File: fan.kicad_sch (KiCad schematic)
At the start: 9 parts, among them J4 Conn_01x04, U7 EMC2101

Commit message: moved all custom symbols and footprints to the bitaxe library
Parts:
- U7: symbol dayminer:EMC2101 -> bitaxe:EMC2101
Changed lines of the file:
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@@
     )
   )
-  (symbol (lib_id "dayminer:EMC2101") (at 144.78 78.105 0) (unit 1)
+  (symbol (lib_id "bitaxe:EMC2101") (at 144.78 78.105 0) (unit 1)
     (in_bom yes) (on_board yes) (dnp no)
     (property "Reference" "U7" (at 153.67 69.215 0)

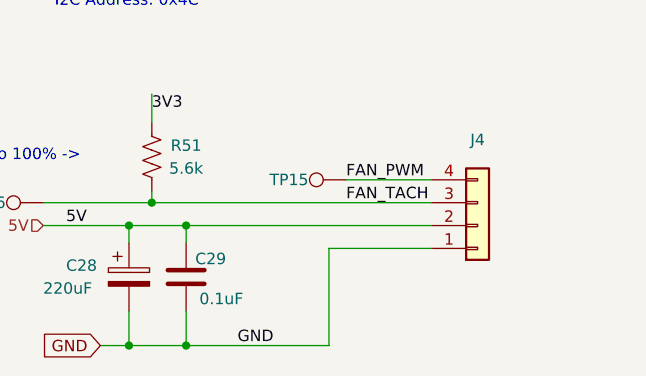
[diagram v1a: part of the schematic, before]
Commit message: Changed barrel plug to 2 pin, added JST-XH connector
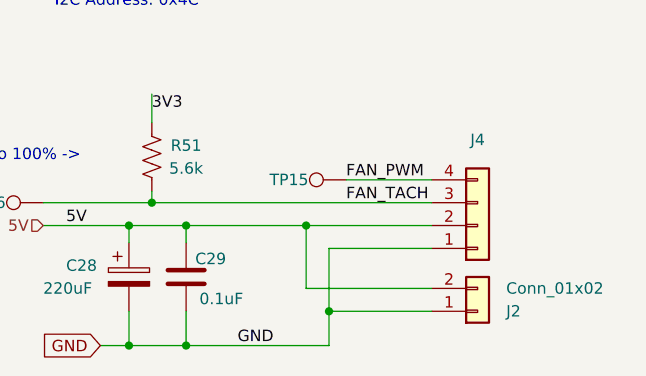
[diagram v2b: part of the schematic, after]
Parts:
- added J2: Conn_01x02, Connector_JST:JST_XH_B2B-XH-A_1x02_P2.50mm_Vertical, symbol Connector_Generic:Conn_01x02
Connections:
- net 5V: now also J2.2 (Pin_2)
- net GND: now also J2.1 (Pin_1)
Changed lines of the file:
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@@
   (junction (at 191.77 66.04) (diameter 0) (color 0 0 0 0)
   )
+  (junction (at 164.465 113.665) (diameter 0) (color 0 0 0 0)
+  )
   (junction (at 151.13 113.665) (diameter 0) (color 0 0 0 0)
+  )
+  (junction (at 167.005 123.19) (diameter 0) (color 0 0 0 0)
   )
   (junction (at 147.32 111.125) (diameter 0) (color 0 0 0 0)
@@
     (stroke (width 0) (type default))
   )
+  (wire (pts (xy 178.435 120.65) (xy 164.465 120.65))
+    (stroke (width 0) (type default))
+  )
   (wire (pts (xy 179.07 66.04) (xy 191.77 66.04))
     (stroke (width 0) (type default))
@@
     (stroke (width 0) (type default))
   )
-  (wire (pts (xy 167.005 116.205) (xy 167.005 127))
+  (wire (pts (xy 167.005 116.205) (xy 167.005 123.19))
     (stroke (width 0) (type default))
   )
@@
     (stroke (width 0) (type default))
   )
+  (wire (pts (xy 167.005 123.19) (xy 167.005 127))
+    (stroke (width 0) (type default))
+  )
+  (wire (pts (xy 167.005 123.19) (xy 178.435 123.19))
+    (stroke (width 0) (type default))
+  )
   (wire (pts (xy 191.77 81.28) (xy 191.77 83.185))
     (stroke (width 0) (type default))
@@
     (stroke (width 0) (type default))
   )
+  (wire (pts (xy 164.465 113.665) (xy 178.435 113.665))
+    (stroke (width 0) (type default))
+  )
   (wire (pts (xy 151.13 113.665) (xy 151.13 115.57))
     (stroke (width 0) (type default))
@@
     (stroke (width 0) (type default))
   )
-  (wire (pts (xy 151.13 113.665) (xy 178.435 113.665))
+  (wire (pts (xy 151.13 113.665) (xy 164.465 113.665))
     (stroke (width 0) (type default))
   )
@@
   )
   (wire (pts (xy 141.605 127) (xy 144.78 127))
+    (stroke (width 0) (type default))
+  )
+  (wire (pts (xy 164.465 120.65) (xy 164.465 113.665))
     (stroke (width 0) (type default))
   )
@@
         )
       )
+    )
+  )
+  (symbol (lib_id "Connector_Generic:Conn_01x02") (at 183.515 123.19 0) (mirror x) (unit 1)
+    (in_bom yes) (on_board yes) (dnp no)
+    (property "Reference" "J2" (at 186.69 123.19 0)
+      (effects (font (size 1.27 1.27)) (justify left))
+    )
+    (property "Value" "Conn_01x02" (at 186.69 120.65 0)
+      (effects (font (size 1.27 1.27)) (justify left))
+    )
+    (property "Footprint" "Connector_JST:JST_XH_B2B-XH-A_1x02_P2.50mm_Vertical" (at 183.515 123.19 0)
+      (effects (font (size 1.27 1.27)) hide)
+    )
+    (property "Datasheet" "https://www.jst-mfg.com/product/pdf/eng/eXH.pdf" (at 183.515 123.19 0)
+      (effects (font (size 1.27 1.27)) hide)
+    )
+    (property "DK" "https://www.digikey.com/en/products/detail/jst-sales-america-inc/B2B-XH-A/1651045" (at 183.515 123.19 0)
+      (effects (font (size 1.27 1.27)) hide)
+    )
+    (pin "1")
+    (pin "2")
+    (instances
+      (project "bitaxeUltra"
+        (path "/e63e39d7-6ac0-4ffd-8aa3-1841a4541b55/8e8832ea-6bf1-49d2-b3a5-32a207f555d2"
+          (reference "J2") (unit 1)
+        )
+      )

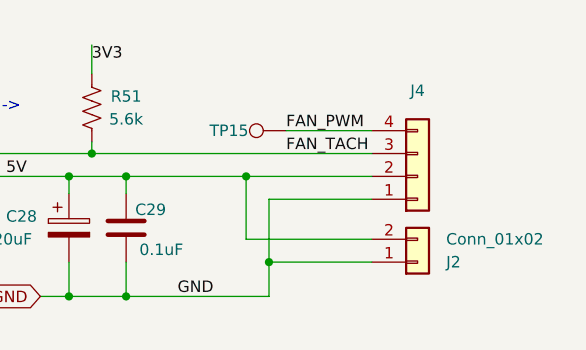
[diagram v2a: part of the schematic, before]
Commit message: fix JSX, updated boms
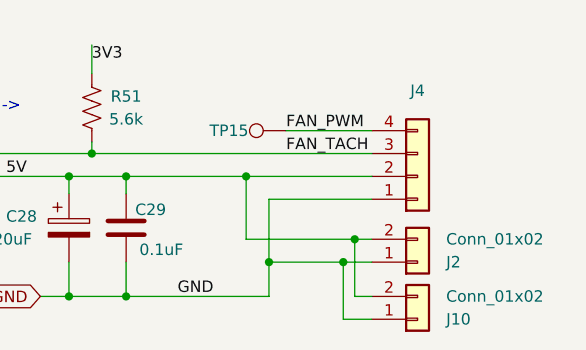
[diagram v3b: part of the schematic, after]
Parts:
- added J10: Conn_01x02, Connector_JST:JST_XH_B2B-XH-A_1x02_P2.50mm_Vertical, symbol Connector_Generic:Conn_01x02
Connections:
- net 5V: now also J10.2 (Pin_2)
- net GND: now also J10.1 (Pin_1)
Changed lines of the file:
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@@
     (rev "0")
   )
+  (junction (at 175.26 123.19) (diameter 0) (color 0 0 0 0)
+  )
   (junction (at 191.77 66.04) (diameter 0) (color 0 0 0 0)
   )
   (junction (at 164.465 113.665) (diameter 0) (color 0 0 0 0)
+  )
+  (junction (at 176.53 120.65) (diameter 0) (color 0 0 0 0)
   )
   (junction (at 151.13 113.665) (diameter 0) (color 0 0 0 0)
@@
     (stroke (width 0) (type default))
   )
-  (wire (pts (xy 178.435 120.65) (xy 164.465 120.65))
+  (wire (pts (xy 178.435 120.65) (xy 176.53 120.65))
     (stroke (width 0) (type default))
   )
@@
     (stroke (width 0) (type default))
   )
+  (wire (pts (xy 164.465 120.65) (xy 176.53 120.65))
+    (stroke (width 0) (type default))
+  )
   (wire (pts (xy 167.005 116.205) (xy 167.005 123.19))
     (stroke (width 0) (type default))
@@
     (stroke (width 0) (type default))
   )
-  (wire (pts (xy 167.005 123.19) (xy 178.435 123.19))
+  (wire (pts (xy 167.005 123.19) (xy 175.26 123.19))
     (stroke (width 0) (type default))
   )
@@
     (stroke (width 0) (type default))
   )
+  (wire (pts (xy 178.435 129.54) (xy 175.26 129.54))
+    (stroke (width 0) (type default))
+  )
   (wire (pts (xy 191.77 66.04) (xy 191.77 73.66))
     (stroke (width 0) (type default))
@@
     (stroke (width 0) (type default))
   )
+  (wire (pts (xy 175.26 123.19) (xy 178.435 123.19))
+    (stroke (width 0) (type default))
+  )
   (wire (pts (xy 164.465 120.65) (xy 164.465 113.665))
     (stroke (width 0) (type default))
   )
+  (wire (pts (xy 178.435 127) (xy 176.53 127))
+    (stroke (width 0) (type default))
+  )
   (wire (pts (xy 144.78 113.665) (xy 144.78 115.57))
     (stroke (width 0) (type default))
   )
   (wire (pts (xy 151.13 127) (xy 167.005 127))
+    (stroke (width 0) (type default))
+  )
+  (wire (pts (xy 175.26 123.19) (xy 175.26 129.54))
+    (stroke (width 0) (type default))
+  )
+  (wire (pts (xy 176.53 120.65) (xy 176.53 127))
     (stroke (width 0) (type default))
   )
@@
         )
       )
+    )
+  )
+  (symbol (lib_id "Connector_Generic:Conn_01x02") (at 183.515 129.54 0) (mirror x) (unit 1)
+    (in_bom yes) (on_board yes) (dnp no)
+    (property "Reference" "J10" (at 186.69 129.54 0)
+      (effects (font (size 1.27 1.27)) (justify left))
+    )
+    (property "Value" "Conn_01x02" (at 186.69 127 0)
+      (effects (font (size 1.27 1.27)) (justify left))
+    )
+    (property "Footprint" "Connector_JST:JST_XH_B2B-XH-A_1x02_P2.50mm_Vertical" (at 183.515 129.54 0)
+      (effects (font (size 1.27 1.27)) hide)
+    )
+    (property "Datasheet" "https://www.jst-mfg.com/product/pdf/eng/eXH.pdf" (at 183.515 129.54 0)
+      (effects (font (size 1.27 1.27)) hide)
+    )
+    (property "DK" "https://www.digikey.com/en/products/detail/jst-sales-america-inc/B2B-XH-A/1651045" (at 183.515 129.54 0)
+      (effects (font (size 1.27 1.27)) hide)
+    )
+    (pin "1")
+    (pin "2")
+    (instances
+      (project "bitaxeUltra"
+        (path "/e63e39d7-6ac0-4ffd-8aa3-1841a4541b55/8e8832ea-6bf1-49d2-b3a5-32a207f555d2"
+          (reference "J10") (unit 1)
+        )
+      )

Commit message: added polarity marker for #82 updated bitaxe logo
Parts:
- J10, J2: footprint Connector_JST:JST_XH_B2B-XH-A_1x02_P2.50mm_Vertical -> bitaxe:JST_XH_B2B-XH-A_1x02_P2.50mm_Vertical
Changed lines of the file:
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@@
       (effects (font (size 1.27 1.27)) (justify left))
     )
-    (property "Footprint" "Connector_JST:JST_XH_B2B-XH-A_1x02_P2.50mm_Vertical" (at 183.515 129.54 0)
+    (property "Footprint" "bitaxe:JST_XH_B2B-XH-A_1x02_P2.50mm_Vertical" (at 183.515 129.54 0)
       (effects (font (size 1.27 1.27)) hide)
     )
@@
       (effects (font (size 1.27 1.27)) (justify left))
     )
-    (property "Footprint" "Connector_JST:JST_XH_B2B-XH-A_1x02_P2.50mm_Vertical" (at 183.515 123.19 0)
+    (property "Footprint" "bitaxe:JST_XH_B2B-XH-A_1x02_P2.50mm_Vertical" (at 183.515 123.19 0)
       (effects (font (size 1.27 1.27)) hide)
     )

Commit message: cleanup
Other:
- title: le bitaxeUltra -> BM1366 bitaxe
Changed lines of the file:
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@@
   (paper "A")
   (title_block
-    (title "le bitaxeUltra")
-    (date "2023-07-10")
-    (rev "0")
+    (title "BM1366 bitaxe")
+    (date "2023-10-10")
+    (rev "1.1")
   )
   (junction (at 175.26 123.19) (diameter 0) (color 0 0 0 0)

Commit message: added missing part numbers. updated BOM and iBOM
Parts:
- J10: DK https://www.digikey.com/en/products/detail/jst-sales-americ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 -> 455-B2B-XH-A-ND; PARTNO (none) -> B2B-XH-A; now left out of the parts list
- J2: DK https://www.digikey.com/en/products/detail/jst-sales-americ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 -> 455-B2B-XH-A-ND; PARTNO (none) -> B2B-XH-A
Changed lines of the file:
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@@
   )
   (symbol (lib_id "Connector_Generic:Conn_01x02") (at 183.515 129.54 0) (mirror x) (unit 1)
-    (in_bom yes) (on_board yes) (dnp no)
+    (in_bom no) (on_board yes) (dnp no)
     (property "Reference" "J10" (at 186.69 129.54 0)
       (effects (font (size 1.27 1.27)) (justify left))
@@
       (effects (font (size 1.27 1.27)) hide)
     )
-    (property "DK" "https://www.digikey.com/en/products/detail/jst-sales-america-inc/B2B-XH-A/1651045" (at 183.515 129.54 0)
+    (property "DK" "455-B2B-XH-A-ND" (at 183.515 129.54 0)
+      (effects (font (size 1.27 1.27)) hide)
+    )
+    (property "PARTNO" "B2B-XH-A" (at 183.515 129.54 0)
       (effects (font (size 1.27 1.27)) hide)
     )
@@
       (effects (font (size 1.27 1.27)) hide)
     )
-    (property "DK" "https://www.digikey.com/en/products/detail/jst-sales-america-inc/B2B-XH-A/1651045" (at 183.515 123.19 0)
+    (property "DK" "455-B2B-XH-A-ND" (at 183.515 123.19 0)
       (effects (font (size 1.27 1.27)) hide)
     )
+    (property "PARTNO" "B2B-XH-A" (at 183.515 123.19 0)
+      (effects (font (size 1.27 1.27)) hide)
+    )
